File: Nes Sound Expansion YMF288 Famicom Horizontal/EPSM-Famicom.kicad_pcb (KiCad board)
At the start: 2 copper layers, 99 x 91.7 mm, 40 parts, among them J1 CARTRIDGE_F, J2 CONSOLE_M, J3 OUT_1, J4 EPSM_ADDRESSING, U1 BU9480F, U10 74LS174, U2 LM321, U3 YMF288, U4 74LS132, U5 74LS139, U6 74LS257, U7 74LS257, U8 74LS257, U9 74LS174, X1 SG-8002CA

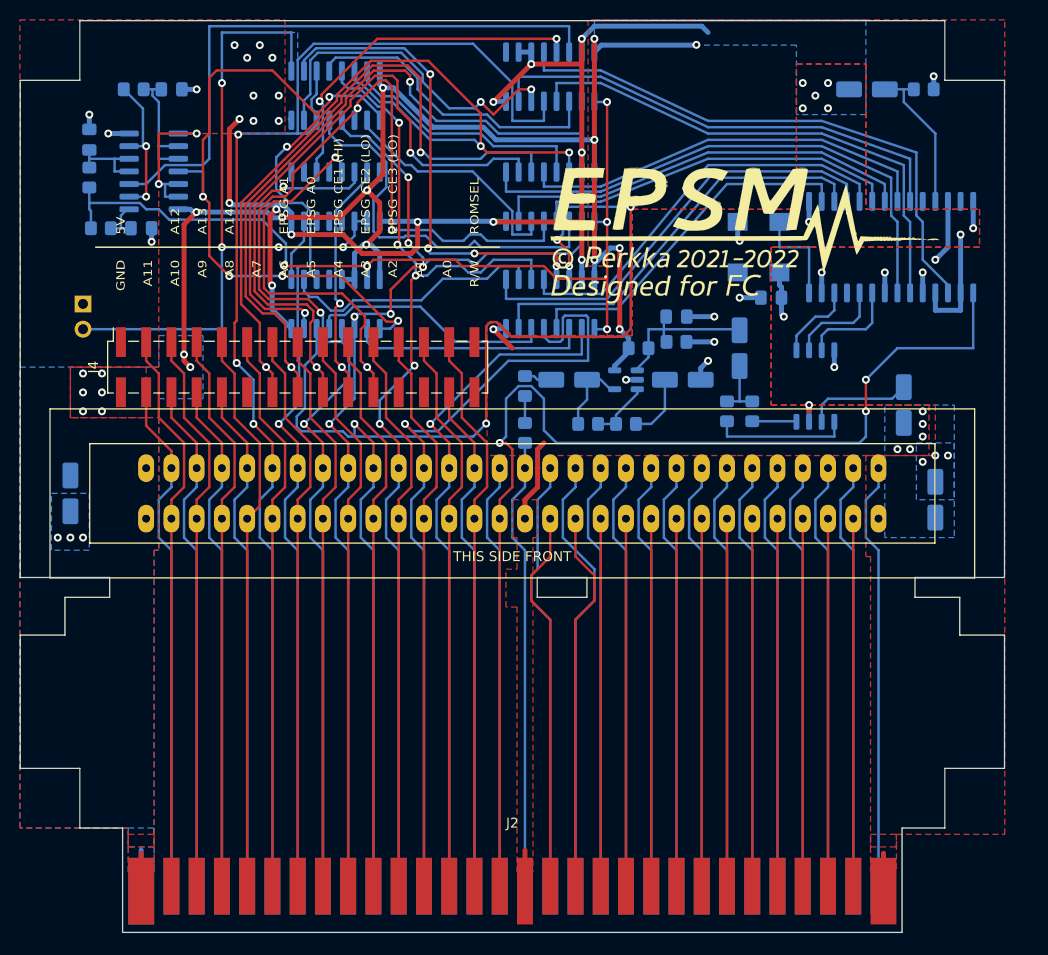
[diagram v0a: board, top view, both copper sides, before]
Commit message: Update FC-H EPSM
- Upgrade to 4 layers
- Use same amplifier circuit as NES EPSM
- Optimize logic chip pin assignment
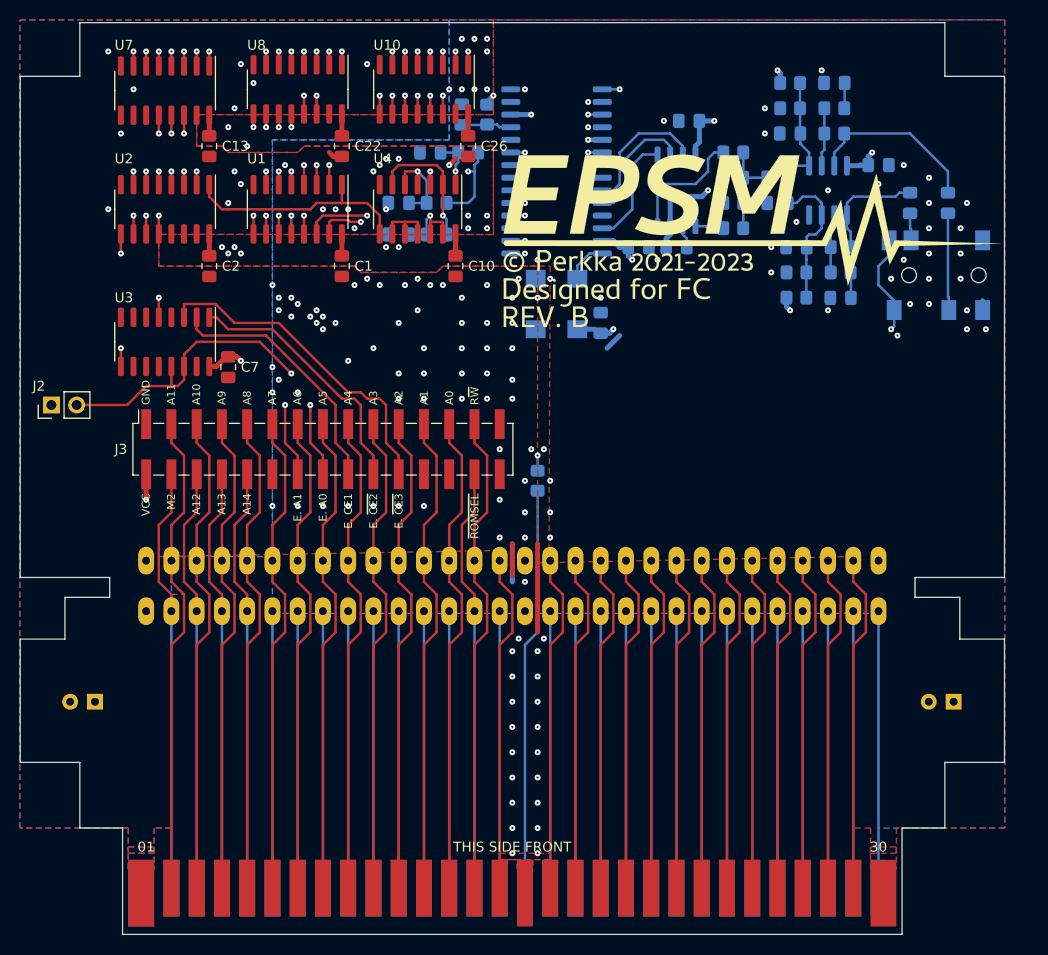
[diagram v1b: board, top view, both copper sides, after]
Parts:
- removed the J4 at (105.4, 80.6)
- removed the Ref** at (127.0, 91.4)
- added C13: 0.1uF, Capacitor_SMD:C_0805_2012Metric_Pad1.18x1.45mm_HandSolder, F.Cu at (96.5, 58.4)
- added C14: 100uF, Capacitor_THT:CP_Radial_D5.0mm_P2.50mm, B.Cu at (85.0, 114.3)
- added C15: 100uF, Capacitor_THT:CP_Radial_D5.0mm_P2.50mm, B.Cu at (171.4, 114.3)
- added C16: 10uF, Capacitor_SMD:C_0805_2012Metric_Pad1.18x1.45mm_HandSolder, B.Cu at (153.7, 64.1)
- added C17: 10uF, Capacitor_SMD:C_0805_2012Metric_Pad1.18x1.45mm_HandSolder, B.Cu at (153.7, 61.6)
- added C18: 68pF, Capacitor_SMD:C_0805_2012Metric_Pad1.18x1.45mm_HandSolder, B.Cu at (155.6, 68.6)
- added C19: 68pF, Capacitor_SMD:C_0805_2012Metric_Pad1.18x1.45mm_HandSolder, B.Cu at (154.9, 57.1)
- added C20: 10uF, Capacitor_SMD:C_0805_2012Metric_Pad1.18x1.45mm_HandSolder, B.Cu at (160.0, 73.7)
- added C21: 10uF, Capacitor_SMD:C_0805_2012Metric_Pad1.18x1.45mm_HandSolder, B.Cu at (159.4, 52.1)
- added C22: 0.1uF, Capacitor_SMD:C_0805_2012Metric_Pad1.18x1.45mm_HandSolder, F.Cu at (109.9, 58.4)
- added C23: 0.1uF, Capacitor_SMD:C_0805_2012Metric_Pad1.18x1.45mm_HandSolder, B.Cu at (163.8, 60.3)
- added C24: 10uF, Capacitor_SMD:C_0805_2012Metric_Pad1.18x1.45mm_HandSolder, B.Cu at (167.0, 64.1)
- added C25: 10uF, Capacitor_SMD:C_0805_2012Metric_Pad1.18x1.45mm_HandSolder, B.Cu at (170.8, 64.1)
- added C26: 0.1uF, Capacitor_SMD:C_0805_2012Metric_Pad1.18x1.45mm_HandSolder, F.Cu at (122.6, 58.4)
- added J2: OUT_1, Connector_PinHeader_2.54mm:PinHeader_1x02_P2.54mm_Vertical, F.Cu at (80.6, 84.5)
- added J5: AudioJack4_SwitchTR1, EPSM-Famicom:Jack_3.5mm_PJ311_Horizontal, B.Cu at (176.5, 71.4)
- added R13: 8.2K, Resistor_SMD:R_0805_2012Metric_Pad1.20x1.40mm_HandSolder, B.Cu at (160.0, 71.1)
- added R14: 8.2K, Resistor_SMD:R_0805_2012Metric_Pad1.20x1.40mm_HandSolder, B.Cu at (159.4, 54.6)
- added R15: 22K, Resistor_SMD:R_0805_2012Metric_Pad1.20x1.40mm_HandSolder, B.Cu at (160.0, 68.6)
- added R16: 22K, Resistor_SMD:R_0805_2012Metric_Pad1.20x1.40mm_HandSolder, B.Cu at (159.4, 57.1)
- added R17: 1K, Resistor_SMD:R_0805_2012Metric_Pad1.20x1.40mm_HandSolder, B.Cu at (129.5, 92.1)
- added Ref**: Val**, EPSM-Famicom:EPSM_silkscreen, F.Cu at (151.1, 67.9)
- C1, C10: value 68pF -> 0.1uF; moved to F.Cu
- C11, C6: footprint Capacitor_SMD:CP_Elec_4x5.3 -> Capacitor_SMD:C_0805_2012Metric_Pad1.18x1.45mm_HandSolder
- C12: value 10uF -> 0.1uF; footprint Capacitor_SMD:CP_Elec_4x5.3 -> Capacitor_SMD:C_0805_2012Metric_Pad1.18x1.45mm_HandSolder
- C2, C7: value 10uF -> 0.1uF; footprint Capacitor_SMD:CP_Elec_4x5.3 -> Capacitor_SMD:C_0805_2012Metric_Pad1.18x1.45mm_HandSolder; moved to F.Cu
- C3, C4: value 10uF -> 68pF; footprint Capacitor_SMD:CP_Elec_4x5.3 -> Capacitor_SMD:C_0805_2012Metric_Pad1.18x1.45mm_HandSolder
- C8: value 68pF -> 0.1uF
- J1: moved to B.Cu
- J3: value OUT_1 -> EPSM_ADDRESSING; footprint Connector_PinHeader_2.54mm:PinHeader_1x02_P2.54mm_Vertical -> Connector_PinSocket_2.54mm:PinSocket_2x15_P2.54mm_Vertical_SMD; moved to F.Cu
- R10, R12, R9: value 1K -> 47K
- R11: value 3K -> 47K
- R2, R8: value 47K -> 3K
- R4: value 47K -> 1K
- R5: value 1K -> 680
- R7: value 4.7K -> 680
- U1: value BU9480F -> 74LS174; footprint Package_SO:SOIC-8_5.275x5.275mm_P1.27mm -> Package_SO:SOIC-16_3.9x9.9mm_P1.27mm; moved to F.Cu
- U10: value 74LS174 -> 74LS257; moved to F.Cu
- U2: value LM321 -> 74LS174; footprint Package_TO_SOT_SMD:SOT-23-5 -> Package_SO:SOIC-16_3.9x9.9mm_P1.27mm; moved to F.Cu
- U3: value YMF288 -> 74LS139; footprint EPSM-Famicom:SOP-28_7.5x12.8mm_P1.27mm -> Package_SO:SOIC-16_3.9x9.9mm_P1.27mm; moved to F.Cu
- U4, U7, U8: moved to F.Cu
- U5: value 74LS139 -> YMF288; footprint Package_SO:SOIC-16_3.9x9.9mm_P1.27mm -> EPSM-Famicom:SOP-28_7.5x12.8mm_P1.27mm
- U6: value 74LS257 -> BU9480F; footprint Package_SO:SOIC-16_3.9x9.9mm_P1.27mm -> Package_SO:SOIC-8_5.275x5.275mm_P1.27mm
- U9: value 74LS174 -> LM358; footprint Package_SO:SOIC-16_3.9x9.9mm_P1.27mm -> Package_SO:SOIC-8_3.9x4.9mm_P1.27mm
- moved U3 73.6 mm to (92.1, 78.1)
- moved C12 72.6 mm to (144.8, 55.9), turned to 0 degrees
- moved C2 71.2 mm to (96.5, 70.5), turned to 90 degrees
- moved R11 71.1 mm to (154.9, 52.1), turned to 0 degrees
- moved R10 70.1 mm to (155.6, 71.1), turned to 180 degrees
- moved C7 70.1 mm to (98.4, 80.6), turned to 90 degrees
- moved R12 66.0 mm to (154.9, 54.6), turned to 180 degrees
- moved U1 55.0 mm to (105.4, 64.8), turned to -90 degrees
- moved C9 54.6 mm to (135.9, 76.2)
- moved U9 50.8 mm to (158.8, 62.9)
- moved C8 50.1 mm to (139.7, 68.6), turned to 180 degrees
- moved U2 49.4 mm to (92.1, 64.8), turned to -90 degrees
- moved C1 43.3 mm to (109.9, 70.5), turned to 90 degrees
- moved U7 40.2 mm to (92.1, 52.8), turned to -90 degrees
- moved C3 36.8 mm to (118.7, 59.1), turned to 180 degrees
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- renumbered J2 to J4
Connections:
- C1 pad 1: /VCC -> /GND
- C1 pad 2: /GND -> /VCC
- C10 pad 1: Net-(C10-Pad1) -> /GND
- C10 pad 2: /GND -> /VCC
- C11 pad 1: /VCC -> Net-(C11-Pad1)
- C12 pad 1: /VCC -> /GND
- C12 pad 2: /GND -> /VCC
- C2 pad 1: Net-(C2-Pad1) -> /GND
- C2 pad 2: /GND -> /VCC
- C3 pad 2: Net-(C3-Pad2) -> /GND
- C4 pad 2: Net-(C4-Pad2) -> /GND
- C5 pad 1: Net-(C3-Pad2) -> Net-(C5-Pad1)
- C6 pad 1: Net-(C6-Pad1) -> /GND
- C6 pad 2: /GND -> Net-(C6-Pad2)
- C7 pad 2: Net-(C7-Pad2) -> /VCC
- C8 pad 1: Net-(C8-Pad1) -> /GND
- C8 pad 2: /GND -> /VCC
- C9 pad 1: Net-(C9-Pad1) -> /VCC
- J3 pad 2: /OUT_1 -> /VCC
- J4 pad 46: /AUD_RF -> /AUD_EPSM
- R1 pad 1: Net-(C3-Pad1) -> /$4016_EN
- R1 pad 2: Net-(R1-Pad2) -> Net-(C3-Pad1)
- R10 pad 1: /$4016_EN -> Net-(C16-Pad2)
- R10 pad 2: Net-(C8-Pad1) -> /GND
- R11 pad 1: /$4016_EN -> /VCC
- R11 pad 2: Net-(C9-Pad1) -> Net-(C17-Pad2)
- R12 pad 1: Net-(R12-Pad1) -> Net-(C17-Pad2)
- R12 pad 2: Net-(C10-Pad1) -> /GND
- R2 pad 1: /VCC -> /$4016_EN
- R2 pad 2: Net-(C3-Pad2) -> Net-(C4-Pad1)
- R3 pad 1: Net-(C4-Pad2) -> Net-(R3-Pad1)
- R3 pad 2: /AUD_EPSM -> Net-(C5-Pad1)
- R4 pad 1: Net-(C3-Pad2) -> /VCC
- R4 pad 2: /GND -> Net-(C6-Pad2)
- R5 pad 1: Net-(R5-Pad1) -> Net-(C16-Pad1)
- R5 pad 2: Net-(C3-Pad1) -> Net-(R5-Pad2)
- R6 pad 1: /AUD_EPSM -> Net-(C16-Pad1)
- R7 pad 1: Net-(C6-Pad1) -> Net-(C17-Pad1)
- R8 pad 1: Net-(R7-Pad2) -> Net-(C17-Pad1)
- R8 pad 2: Net-(C4-Pad1) -> /AUD_RF
- R9 pad 2: Net-(C7-Pad2) -> Net-(C16-Pad2)
- U1 pad 1: Net-(R1-Pad2) -> /FF_RESET
- U1 pad 2: Net-(C2-Pad1) -> /BUF_A0
- U1 pad 3: /GND -> /CPU_D3
- U1 pad 4: Net-(R5-Pad1) -> /CPU_D2
- U1 pad 5: Net-(U1-Pad5) -> /BUF_A1
- U1 pad 6: Net-(U1-Pad6) -> /CPU_D7
- U1 pad 7: Net-(U1-Pad7) -> /BUF_D7
- U1 pad 8: /VCC -> /GND
- U10 pad 1: /FF_RESET -> /$4016_EN
- U10 pad 10: /BUF_D3 -> /BUF_D7
- U10 pad 12: /BUF_A1 -> /YM_A1
- U10 pad 13: /CPU_D2 -> /BUF_A0
- U10 pad 14: /CPU_D6 -> /EPSM_A1_A1
- U10 pad 15: /BUF_D6 -> /GND
- U10 pad 2: /BUF_D5 -> /BUF_CS
- U10 pad 3: /CPU_D5 -> /~{CS}
- U10 pad 4: /CPU_D4 -> /YM_CS
- U10 pad 5: /BUF_D4 -> /EPSM_A0_A13
- U10 pad 6: /CPU_D7 -> /BUF_A1
- U10 pad 7: /BUF_D7 -> /YM_A0
- U10 pad 9: /OUT_1 -> /YM_D7
- U2 pad 1: Net-(C3-Pad2) -> /FF_RESET
- U2 pad 2: /GND -> /BUF_D3
- U2 pad 3: Net-(R7-Pad2) -> /CPU_D7
- U2 pad 4: Net-(C4-Pad1) -> /CPU_D6
- U2 pad 5: /VCC -> /BUF_D2
- U3 pad 1: /GND -> /EPSM_CE2_~{ROMSEL}
- U3 pad 11: Net-(C7-Pad2) -> unconnected-(U3-Pad11)
- U3 pad 12: /VCC -> unconnected-(U3-Pad12)
- U3 pad 13: unconnected-(U3-Pad13) -> /OUT_1
- U3 pad 14: /GND -> /OUT_1
- U3 pad 15: /~{IRQ} -> /GND
- U3 pad 16: /GND -> /VCC
- U3 pad 2: /YM_D0 -> /EPSM_CE1_A14
- U3 pad 3: /YM_D1 -> /EPSM_CE3_CPU_R~{W}
- U3 pad 4: /YM_D2 -> unconnected-(U3-Pad4)
- U3 pad 5: /YM_D3 -> /~{CS}
- U3 pad 6: /YM_D4 -> unconnected-(U3-Pad6)
- U3 pad 7: /YM_D5 -> unconnected-(U3-Pad7)
- U3 pad 8: /YM_D6 -> /GND
- U3 pad 9: /YM_D7 -> /~{OUT_1}
- U4 pad 1: Net-(C8-Pad1) -> Net-(C3-Pad1)
- U4 pad 10: Net-(C10-Pad1) -> Net-(U4-Pad10)
- U4 pad 11: /FF_RESET -> Net-(U4-Pad10)
- U4 pad 12: Net-(U4-Pad12) -> Net-(C5-Pad1)
- U4 pad 13: Net-(U4-Pad12) -> Net-(C5-Pad1)
- U4 pad 2: Net-(R12-Pad1) -> Net-(R3-Pad1)
- U4 pad 4: Net-(C9-Pad1) -> Net-(C4-Pad1)
- U4 pad 5: Net-(C9-Pad1) -> Net-(C4-Pad1)
- U4 pad 6: Net-(R12-Pad1) -> Net-(R3-Pad1)
- U4 pad 8: Net-(U4-Pad12) -> /FF_RESET
- U4 pad 9: Net-(C10-Pad1) -> Net-(U4-Pad10)
- U5 pad 11: /~{CS} -> Net-(C6-Pad2)
- U5 pad 12: unconnected-(U5-Pad12) -> /VCC
- U5 pad 13: /EPSM_CE3_CPU_R~{W} -> unconnected-(U5-Pad13)
- U5 pad 14: /EPSM_CE1_A14 -> /GND
- U5 pad 15: /EPSM_CE2_~{ROMSEL} -> /~{IRQ}
- U5 pad 16: /VCC -> /GND
- U5 pad 2: /OUT_1 -> /YM_D0
- U5 pad 3: /OUT_1 -> /YM_D1
- U5 pad 4: unconnected-(U5-Pad4) -> /YM_D2
- U5 pad 5: unconnected-(U5-Pad5) -> /YM_D3
- U5 pad 6: unconnected-(U5-Pad6) -> /YM_D4
- U5 pad 7: /~{OUT_1} -> /YM_D5
- U5 pad 8: /GND -> /YM_D6
- U5 pad 9: unconnected-(U5-Pad9) -> /YM_D7
- U6 pad 1: /$4016_EN -> Net-(R5-Pad2)
- U6 pad 2: /CPU_D0 -> Net-(C11-Pad1)
- U6 pad 3: /BUF_D0 -> /GND
- U6 pad 4: /YM_D0 -> Net-(R7-Pad2)
- U6 pad 5: /CPU_D1 -> Net-(U5-Pad26)
- U6 pad 6: /BUF_D1 -> Net-(U5-Pad24)
- U6 pad 7: /YM_D1 -> Net-(U5-Pad23)
- U6 pad 8: /GND -> /VCC
- U7 pad 10: /BUF_A0 -> /GND
- U7 pad 11: /EPSM_A1_A1 -> /GND
- U7 pad 12: /YM_D6 -> /YM_D0
- U7 pad 13: /BUF_D6 -> /BUF_D0
- U7 pad 14: /CPU_D6 -> /CPU_D0
- U7 pad 2: /CPU_D4 -> /CPU_D2
- U7 pad 3: /BUF_D4 -> /BUF_D2
- U7 pad 4: /YM_D4 -> /YM_D2
- U7 pad 5: /CPU_D5 -> /CPU_D1
- U7 pad 6: /BUF_D5 -> /BUF_D1
- U7 pad 7: /YM_D5 -> /YM_D1
- U7 pad 9: /YM_A1 -> unconnected-(U7-Pad9)
- U8 pad 10: /GND -> /BUF_D3
- U8 pad 11: /GND -> /CPU_D3
- U8 pad 12: /YM_CS -> /YM_D4
- U8 pad 13: /~{CS} -> /BUF_D4
- U8 pad 14: /BUF_CS -> /CPU_D4
- U8 pad 2: /EPSM_A0_A13 -> /CPU_D6
- U8 pad 3: /BUF_A1 -> /BUF_D6
- U8 pad 4: /YM_A0 -> /YM_D6
- U8 pad 5: /CPU_D7 -> /CPU_D5
- U8 pad 6: /BUF_D7 -> /BUF_D5
- U8 pad 7: /YM_D7 -> /YM_D5
- U8 pad 9: unconnected-(U8-Pad9) -> /YM_D3
- U9 pad 1: /FF_RESET -> Net-(C24-Pad1)
- U9 pad 2: /BUF_D0 -> Net-(R13-Pad2)
- U9 pad 3: /CPU_D4 -> Net-(C16-Pad2)
- U9 pad 4: /CPU_D5 -> /GND
- U9 pad 5: /BUF_D1 -> Net-(C17-Pad2)
- U9 pad 6: /CPU_D3 -> Net-(R14-Pad2)
- U9 pad 7: /BUF_A0 -> Net-(C25-Pad1)
- U9 pad 8: /GND -> /VCC
- X1 pad 3: Net-(U3-Pad28) -> Net-(U5-Pad28)
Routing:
- net /VCC: track 175.8 -> 46.1 mm, vias 29 -> 17
- net /GND: track 183.4 -> 67.2 mm, vias 48 -> 137
- net Net-(J5-PadR1N): track 0.00 -> 53.7 mm, vias 0 -> 2
- net /CPU_D3: track 132.6 -> 85.3 mm, vias 5 -> 3
- net /FF_RESET: track 69.4 -> 23.3 mm, vias 5 -> 0
- net /BUF_CS: track 61.3 -> 15.8 mm, vias 0 -> 2
- net /BUF_A0: track 58.4 -> 19.2 mm, vias 2 -> 3
- net /AUD_EPSM: track 2.72 -> 40.5 mm
- net /YM_CS: track 56.4 -> 22.0 mm, vias 0 -> 2
- net /BUF_D3: track 48.9 -> 16.8 mm
- net /CPU_D0: track 69.0 -> 96.6 mm, vias 1 -> 2
- net /YM_A1: track 54.2 -> 26.7 mm, vias 0 -> 2
- net /YM_D7: track 47.8 -> 22.5 mm, vias 0 -> 2
- net /~{IRQ}: track 115.2 -> 91.6 mm, vias 3 -> 1
- net /YM_A0: track 51.6 -> 28.5 mm, vias 0 -> 2
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- added copper zone on In1.Cu, net /GND
- added copper zone on In2.Cu, net /GND
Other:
- outline, holes or cut-outs redrawn
- copper layers 2 -> 4
- board text added: "01"
- board text added: "30"
- board text added: "31"
- board text added: "60"
- board text added: "GND A11 A10 A9 A8 A7 A6 A5 A4 A3 A2 A1 A0 R~{W}"
- board text added: "THIS SIDE BACK"
- board text added: "THIS SIDE FRONT"
- board text added: "VCC M2 A12 A13 A14 E. A1 E. A0 E. CE1 E. ~{CE2} E. ~{CE3} ~{ROMSEL}"
- board text removed: "5V A12 A13 A14 EPSG A1 EPSG A0 EPSG CE1 (HI) EPSG CE2 (LO) EPSG CE3 (LO) ROMSEL"
- board text removed: "GND A11 A10 A9 A8 A7 A6 A5 A4 A3 A2 A1 A0 R/W"

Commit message: Reposition all SMD components to be on top
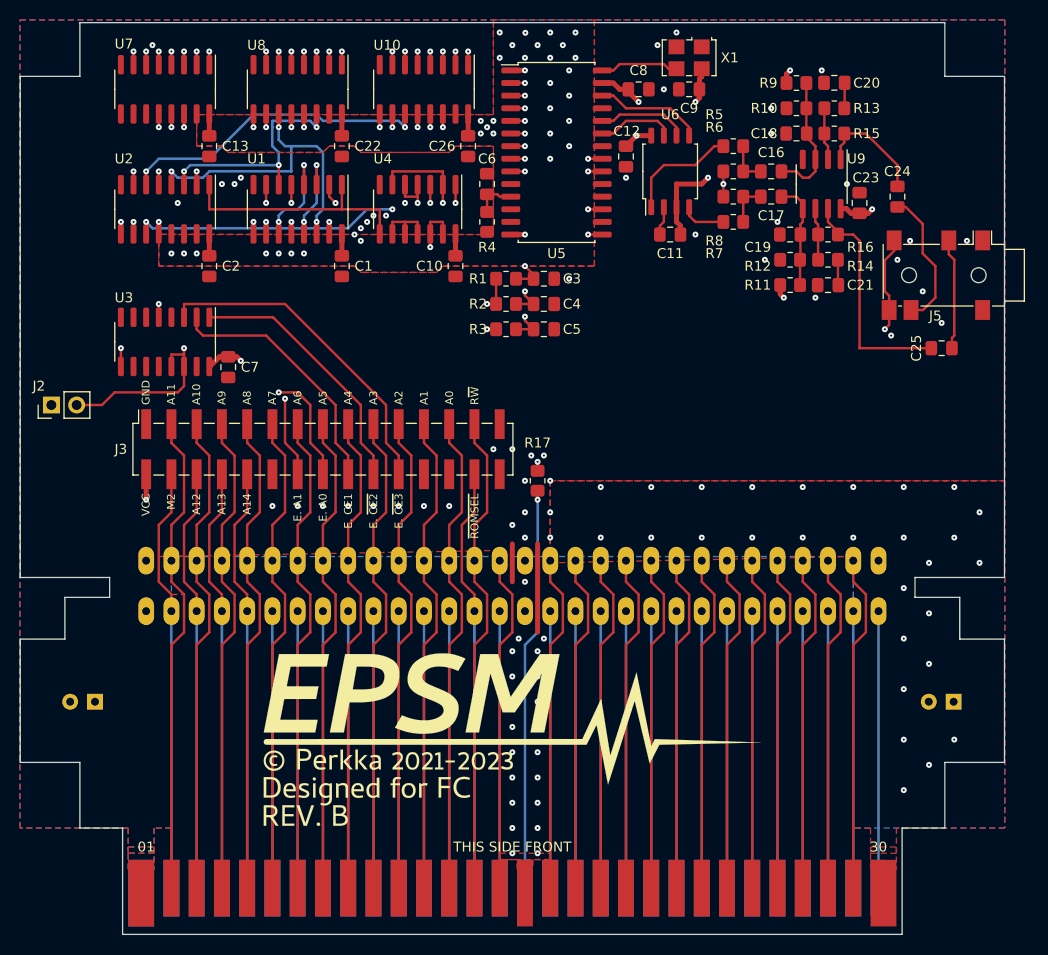
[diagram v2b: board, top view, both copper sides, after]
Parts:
- C11, C12, C16, C17, C18, C19, C20, C21, C23, C24, C25, C3, C4, C5, C6, C8, C9, J5, R1, R10, R11, R12, R13, R14, R15, R16, R17, R2, R3, R4, R5, R6, R7, R8, R9, U5, U6, U9: moved to F.Cu
- X1: footprint Oscillator:Oscillator_SMD_SeikoEpson_SG8002CA-4Pin_7.0x5.0mm -> Oscillator:Oscillator_SMD_SeikoEpson_SG8002LB-4Pin_5.0x3.2mm; moved to F.Cu
- moved Ref** 55.7 mm to (127.0, 118.1)
- moved X1 28.1 mm to (144.8, 49.5), turned to 180 degrees
- moved C9 25.1 mm to (144.8, 52.7), turned to 180 degrees
- moved C20 21.6 mm to (159.4, 52.0)
- moved R9 21.6 mm to (155.6, 52.1)
- moved C21 20.3 mm to (158.8, 72.4)
- moved R11 20.3 mm to (154.9, 72.4)
- moved C4 17.8 mm to (130.2, 74.3), turned to 0 degrees
- moved C5 17.4 mm to (130.2, 76.8), turned to 0 degrees
- moved C3 17.1 mm to (130.2, 71.8), turned to 0 degrees
- moved R13 16.5 mm to (159.4, 54.6)
- moved R10 16.5 mm to (155.6, 54.6)
- moved C8 15.9 mm to (139.7, 52.7)
- moved R14 15.3 mm to (158.8, 69.8)
- moved R12 15.2 mm to (154.9, 69.8)
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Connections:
- U1 pad 14: /CPU_D6 -> /CPU_D7
- U1 pad 15: /BUF_D6 -> /BUF_D3
- U1 pad 2: /BUF_A0 -> /BUF_D0
- U1 pad 3: /CPU_D3 -> /CPU_D4
- U1 pad 4: /CPU_D2 -> /CPU_D5
- U1 pad 5: /BUF_A1 -> /BUF_D1
- U1 pad 6: /CPU_D7 -> /CPU_D6
- U1 pad 7: /BUF_D7 -> /BUF_D2
- U10 pad 10: /BUF_D7 -> /BUF_D3
- U10 pad 11: /CPU_D7 -> /CPU_D3
- U10 pad 12: /YM_A1 -> /YM_D2
- U10 pad 13: /BUF_A0 -> /BUF_D2
- U10 pad 14: /EPSM_A1_A1 -> /CPU_D2
- U10 pad 2: /BUF_CS -> /CPU_D0
- U10 pad 3: /~{CS} -> /BUF_D0
- U10 pad 4: /YM_CS -> /YM_D0
- U10 pad 5: /EPSM_A0_A13 -> /CPU_D1
- U10 pad 6: /BUF_A1 -> /BUF_D1
- U10 pad 7: /YM_A0 -> /YM_D1
- U10 pad 9: /YM_D7 -> /YM_D3
- U2 pad 10: /BUF_D0 -> /BUF_A1
- U2 pad 11: /CPU_D4 -> /CPU_D2
- U2 pad 2: /BUF_D3 -> /BUF_D6
- U2 pad 3: /CPU_D7 -> /CPU_D6
- U2 pad 4: /CPU_D6 -> /CPU_D7
- U2 pad 5: /BUF_D2 -> /BUF_D7
- U2 pad 6: /CPU_D5 -> /CPU_D3
- U2 pad 7: /BUF_D1 -> /BUF_A0
- U7 pad 12: /YM_D0 -> /YM_CS
- U7 pad 13: /BUF_D0 -> /~{CS}
- U7 pad 14: /CPU_D0 -> /BUF_CS
- U7 pad 2: /CPU_D2 -> /EPSM_A1_A1
- U7 pad 3: /BUF_D2 -> /BUF_A0
- U7 pad 4: /YM_D2 -> /YM_A1
- U7 pad 5: /CPU_D1 -> /EPSM_A0_A13
- U7 pad 6: /BUF_D1 -> /BUF_A1
- U7 pad 7: /YM_D1 -> /YM_A0
- U8 pad 10: /BUF_D3 -> /BUF_D7
- U8 pad 11: /CPU_D3 -> /CPU_D7
- U8 pad 12: /YM_D4 -> /YM_D6
- U8 pad 13: /BUF_D4 -> /BUF_D6
- U8 pad 14: /CPU_D4 -> /CPU_D6
- U8 pad 2: /CPU_D6 -> /CPU_D4
- U8 pad 3: /BUF_D6 -> /BUF_D4
- U8 pad 4: /YM_D6 -> /YM_D4
- U8 pad 9: /YM_D3 -> /YM_D7
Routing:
- net /YM_D1: track 52.9 -> 17.9 mm
- net /YM_D2: track 48.9 -> 14.3 mm
- net /YM_D0: track 47.9 -> 13.6 mm
- net /GND: track 67.2 -> 36.9 mm, vias 137 -> 62
- net /~{CS}: track 51.1 -> 21.0 mm, vias 3 -> 2
- net /YM_CS: track 22.0 -> 49.9 mm
- net /YM_A0: track 28.5 -> 55.1 mm
- net /YM_A1: track 26.7 -> 52.4 mm
- net /CPU_D3: track 85.3 -> 110.5 mm, vias 3 -> 2
- net /BUF_CS: track 15.8 -> 37.0 mm, vias 2 -> 3
- net /CPU_D6: track 124.1 -> 104.3 mm, vias 4 -> 3
- net /~{IRQ}: track 91.6 -> 71.9 mm
- net Net-(R3-Pad1): track 13.4 -> 31.3 mm, vias 1 -> 2
- net /YM_D3: track 36.5 -> 19.2 mm
- net /OUT_1: track 49.3 -> 34.7 mm
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- removed copper zone on B.Cu, net /GND

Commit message: Incremental improvements
- Add ground plane around audio traces
- Nudge audio jack for better allowance
- Add stitching vias in audio amplifier zone
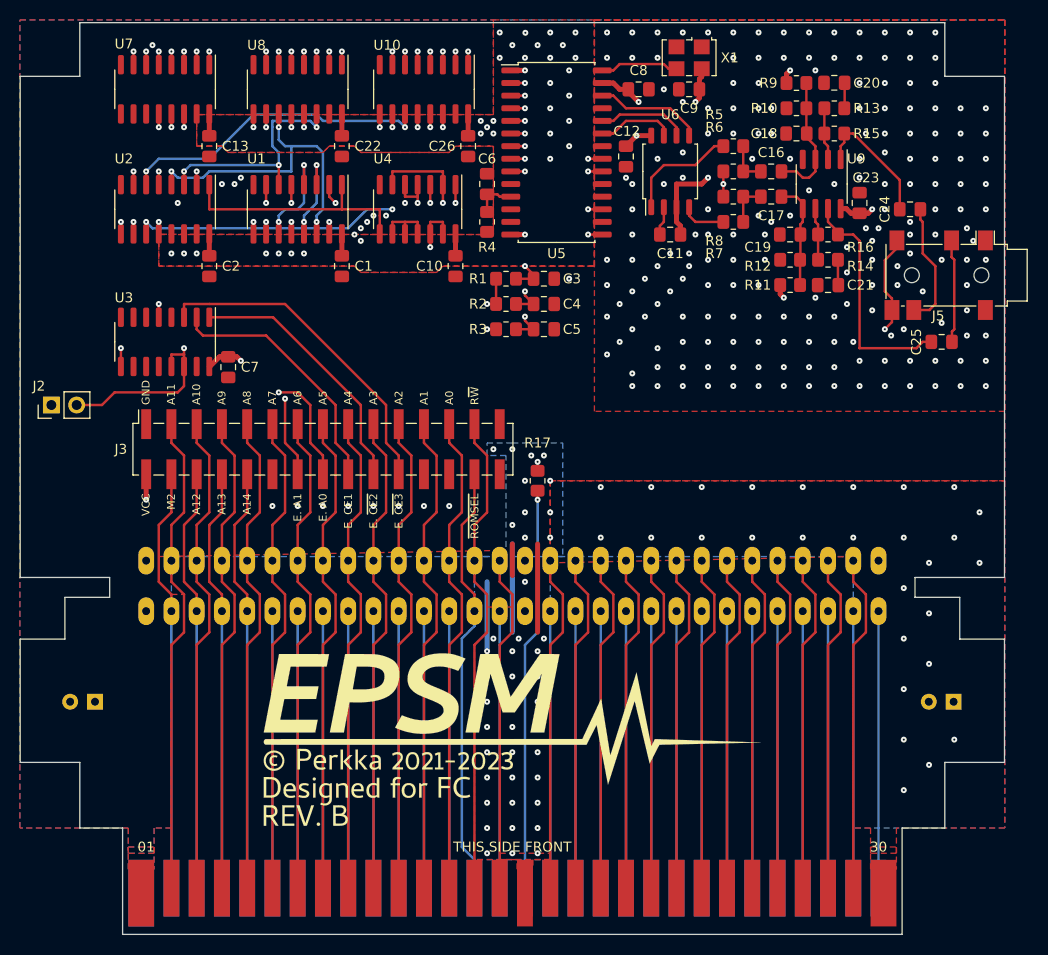
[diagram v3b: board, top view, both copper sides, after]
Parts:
- moved C24 1.80 mm to (167.0, 64.8), turned to 0 degrees
- moved C25 0.63 mm to (170.2, 78.1)
- moved J5 0.28 mm to (176.8, 71.4)
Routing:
- net /GND: track 36.9 -> 52.2 mm, vias 62 -> 244
- net Net-(C24-Pad1): track 11.6 -> 13.2 mm
- net Net-(C24-Pad2): track 14.1 -> 12.6 mm
- net /~{ROMSEL}: track 42.7 -> 43.7 mm
- net Net-(C25-Pad2): track 11.2 -> 10.4 mm
- added copper zone on B.Cu, net /GND
